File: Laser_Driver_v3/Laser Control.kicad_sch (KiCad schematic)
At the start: 10 parts, among them U2 AD5064BRUZ, U20 AD9833xRM, U35 AD9833xRM, U9 74AHCT125

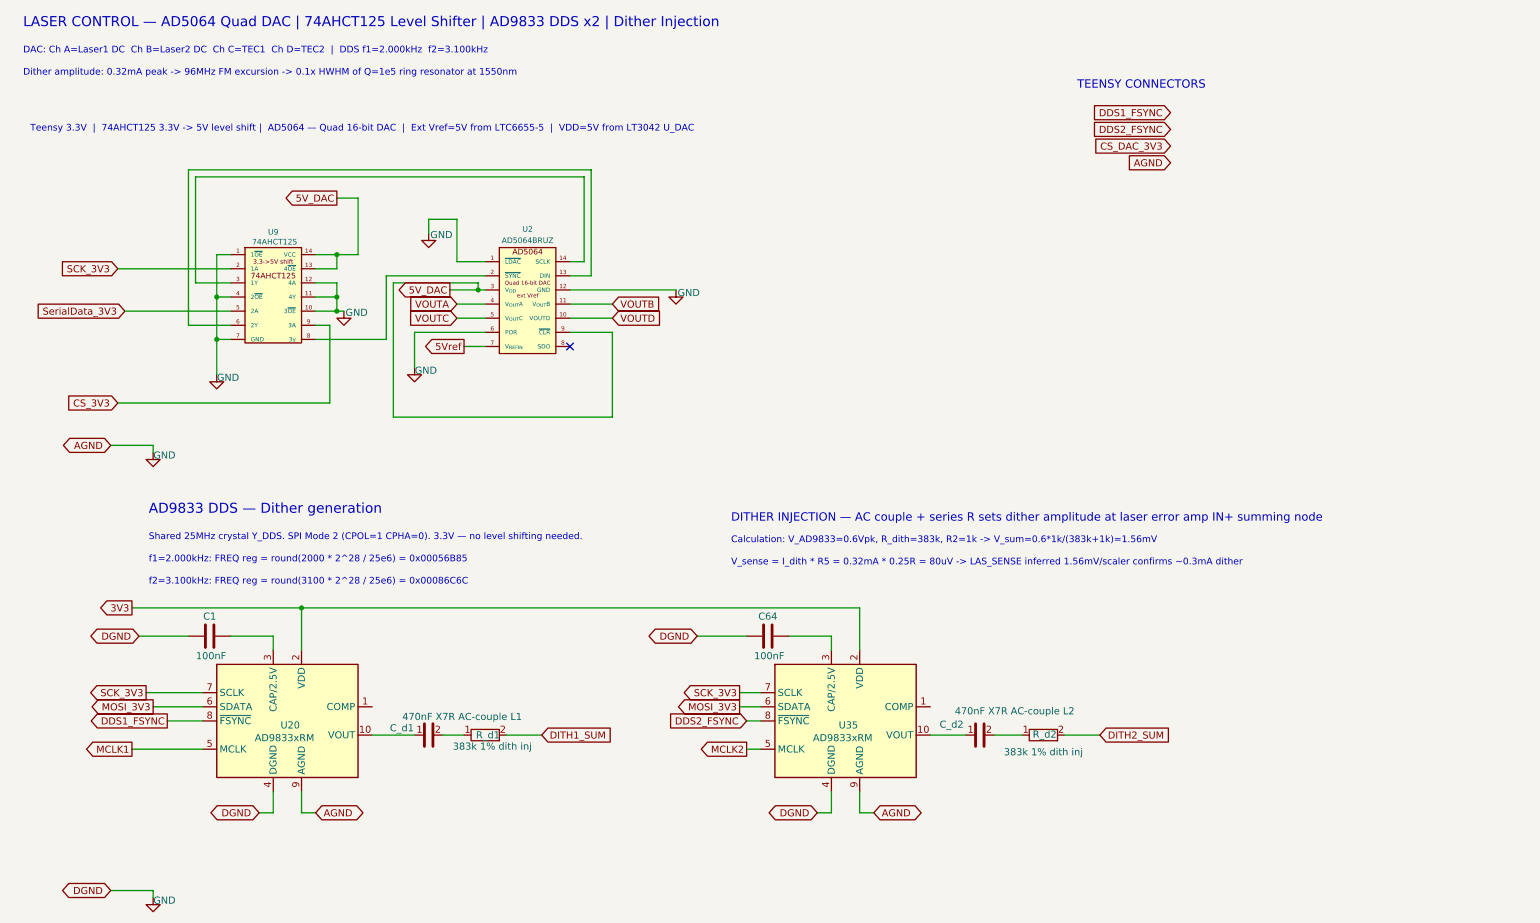
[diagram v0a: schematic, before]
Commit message: First full draft complete.  Added Teensy pinout sheet.
Used Copilot to generate firmware draft.  ** Still need to:  Recheck all specifications and pins, verify design with simulations, go through all footprints, create layout.
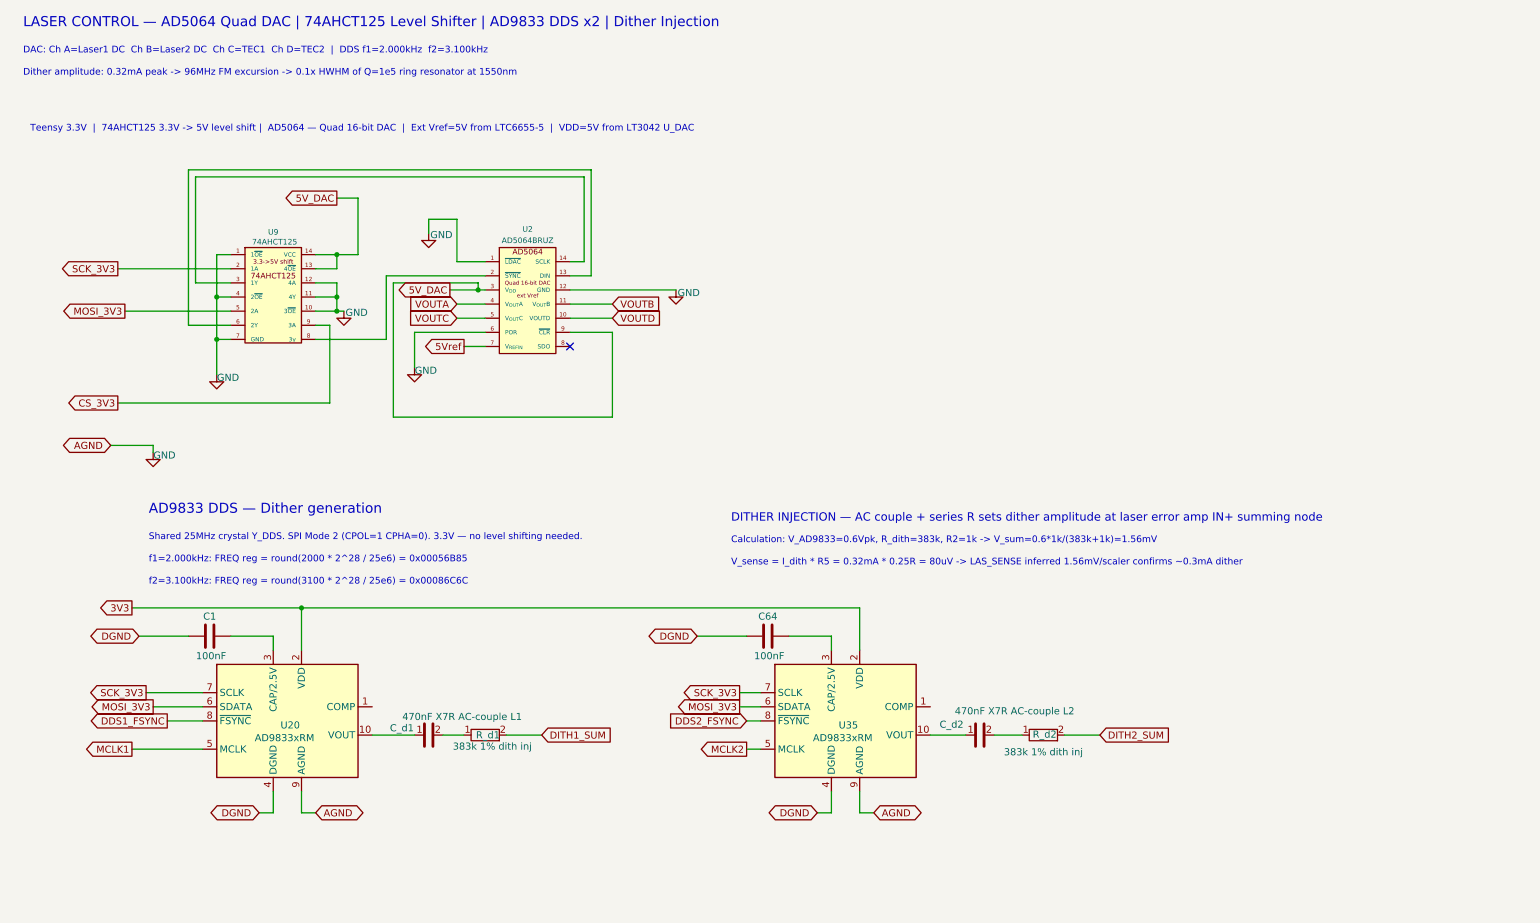
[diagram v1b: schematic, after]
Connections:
- net SerialData_3V3 is gone; now on net MOSI_3V3: U9.5 (2A)
- net GND: no longer C1.1, C64.1, U20.4 (DGND), U35.4 (DGND)
- new net DGND: C1.1, C64.1, U20.4 (DGND), U35.4 (DGND)
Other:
- note removed: "TEENSY CONNECTORS"
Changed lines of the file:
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@@
-		)
-	)
-	(text "TEENSY CONNECTORS"
-		(exclude_from_sim no)
-		(at 202.92 26.7 0)
-		(effects
-			(font
-				(size 1.5 1.5)
-			)
-			(justify left)
 		)
 	)
@@
 	(wire
 		(pts
-			(xy 29.21 171.45) (xy 36.83 171.45)
-		)
-		(stroke
-			(width 0)
-			(type default)
-		)
-	)
-	(wire
-		(pts
 			(xy 50.8 69.85) (xy 43.18 69.85)
 		)
@@
 	(wire
 		(pts
-			(xy 36.83 171.45) (xy 36.83 172.72)
-		)
-		(stroke
-			(width 0)
-			(type default)
-		)
-	)
-	(wire
-		(pts
 			(xy 142.24 135.89) (xy 146.05 135.89)
 		)
@@
 		)
 	)
-	(global_label "SerialData_3V3"
-		(shape input)
+	(global_label "MOSI_3V3"
+		(shape output)
 		(at 31.75 67.31 180)
 		(fields_autoplaced yes)
@@
 		)
 		(property "Intersheetrefs" "${INTERSHEET_REFS}"
-			(at 14.4926 67.31 0)
+			(at 19.6934 67.31 0)
 			(hide yes)
 			(show_name no)
@@
 		)
 	)
-	(global_label "DDS1_FSYNC"
-		(shape input)
-		(at 219.71 31.64 180)
-		(fields_autoplaced yes)
-		(effects
-			(font
-				(size 1.27 1.27)
-			)
-			(justify right)
-		)
-		(property "Intersheetrefs" "${INTERSHEET_REFS}"
-			(at 219.71 31.64 0)
-			(hide yes)
-			(show_name no)
-			(do_not_autoplace no)
-			(effects
-				(font
-					(size 1.27 1.27)
-				)
-				(justify right)
-			)
-		)
-	)
 	(global_label "5Vref"
 		(shape output)
@@
 	)
 	(global_label "CS_3V3"
-		(shape input)
+		(shape output)
 		(at 30.48 83.82 180)
 		(fields_autoplaced yes)
@@
 	)
 	(global_label "SCK_3V3"
-		(shape input)
+		(shape output)
 		(at 30.48 59.69 180)
 		(fields_autoplaced yes)
@@
 	(global_label "DDS2_FSYNC"
 		(shape input)
-		(at 219.71 34.64 180)
+		(at 143.51 140.97 180)
 		(fields_autoplaced yes)
 		(effects
@@
 		)
 		(property "Intersheetrefs" "${INTERSHEET_REFS}"
-			(at 219.71 34.64 0)
-			(hide yes)
-			(show_name no)
-			(do_not_autoplace no)
-			(effects
-				(font
-					(size 1.27 1.27)
-				)
-				(justify right)
-			)
-		)
-	)
-	(global_label "AGND"
-		(shape input)
-		(at 219.71 40.64 180)
-		(fields_autoplaced yes)
-		(effects
-			(font
-				(size 1.27 1.27)
-			)
-			(justify right)
-		)
-		(property "Intersheetrefs" "${INTERSHEET_REFS}"
-			(at 219.71 40.64 0)
-			(hide yes)
-			(show_name no)
-			(do_not_autoplace no)
-			(effects
-				(font
-					(size 1.27 1.27)
-				)
-				(justify right)
-			)
-		)
-	)
-	(global_label "DDS2_FSYNC"
-		(shape input)
-		(at 143.51 140.97 180)
-		(fields_autoplaced yes)
-		(effects
-			(font
-				(size 1.27 1.27)
-			)
-			(justify right)
-		)
-		(property "Intersheetrefs" "${INTERSHEET_REFS}"
 			(at 143.51 140.97 0)
-			(hide yes)
-			(show_name no)
-			(do_not_autoplace no)
-			(effects
-				(font
-					(size 1.27 1.27)
-				)
-				(justify right)
-			)
-		)
-	)
-	(global_label "DGND"
-		(shape bidirectional)
-		(at 29.21 171.45 180)
-		(fields_autoplaced yes)
-		(effects
-			(font
-				(size 1.27 1.27)
-			)
-			(justify right)
-		)
-		(property "Intersheetrefs" "${INTERSHEET_REFS}"
-			(at 19.973 171.45 0)
 			(hide yes)
 			(show_name no)
@@
 				)
 				(justify left)
-			)
-		)
-	)
-	(global_label "CS_DAC_3V3"
-		(shape input)
-		(at 219.71 37.64 180)
-		(fields_autoplaced yes)
-		(effects
-			(font
-				(size 1.27 1.27)
-			)
-			(justify right)
-		)
-		(property "Intersheetrefs" "${INTERSHEET_REFS}"
-			(at 219.71 37.64 0)
-			(hide yes)
-			(show_name no)
-			(do_not_autoplace no)
-			(effects
-				(font
-					(size 1.27 1.27)
-				)
-				(justify right)
 			)
 		)
@@
 					(unit 1)
 				)
-			)
-		)
-	)
-	(symbol
-		(lib_id "power:GND")
-		(at 36.83 172.72 0)
-		(unit 1)
-		(body_style 1)
-		(exclude_from_sim no)
-		(in_bom yes)
-		(on_board yes)
-		(in_pos_files yes)
-		(dnp no)
-		(property "Reference" "#PWR032"
-			(at 36.83 179.07 0)
-			(hide yes)
-			(show_name no)
-			(do_not_autoplace no)
-			(effects
-				(font
-					(size 1.27 1.27)
-				)
-			)
-		)
-		(property "Value" "GND"
-			(at 38.862 173.228 0)
-			(show_name no)
-			(do_not_autoplace no)
-			(effects
-				(font
-					(size 1.27 1.27)
-				)
-			)
-		)
-		(property "Footprint" ""
-			(at 36.83 172.72 0)
-			(hide yes)
-			(show_name no)
-			(do_not_autoplace no)
-			(effects
-				(font
-					(size 1.27 1.27)
-				)
-			)
-		)
-		(property "Datasheet" ""
-			(at 36.83 172.72 0)
-			(hide yes)
-			(show_name no)
-			(do_not_autoplace no)
-			(effects
-				(font
-					(size 1.27 1.27)
-				)
-			)
-		)
-		(property "Description" "Power symbol creates a global label with name \"GND\" , ground"
-			(at 36.83 172.72 0)
-			(hide yes)
-			(show_name no)
-			(do_not_autoplace no)
-			(effects
-				(font
-					(size 1.27 1.27)
-				)
-			)
-		)
-		(pin "1"
-		)
-		(instances
-			(project "laser_driver_v3"
-				(path "/b2c3d4e5-f6a7-8901-bcde-f12345678901/e4d7b089-62e9-414f-b4cc-abd1480c07cf"
-					(reference "#PWR032")
-					(unit 1)
-				)

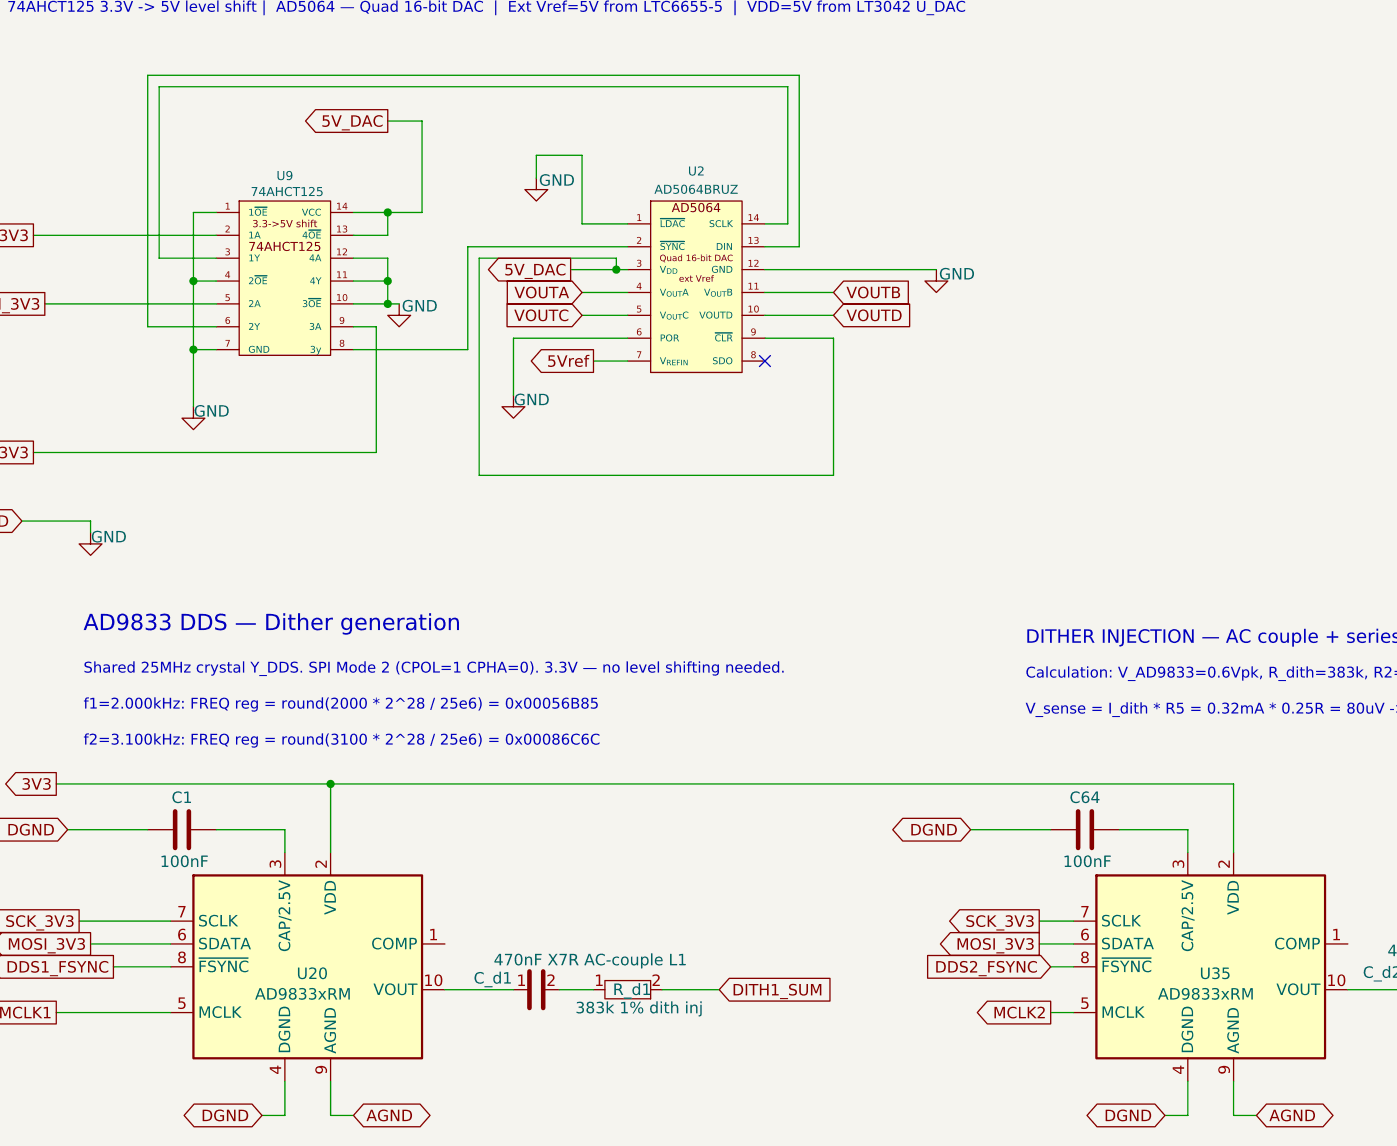
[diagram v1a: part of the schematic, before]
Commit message: Renumbered schematics, corrections, power verified
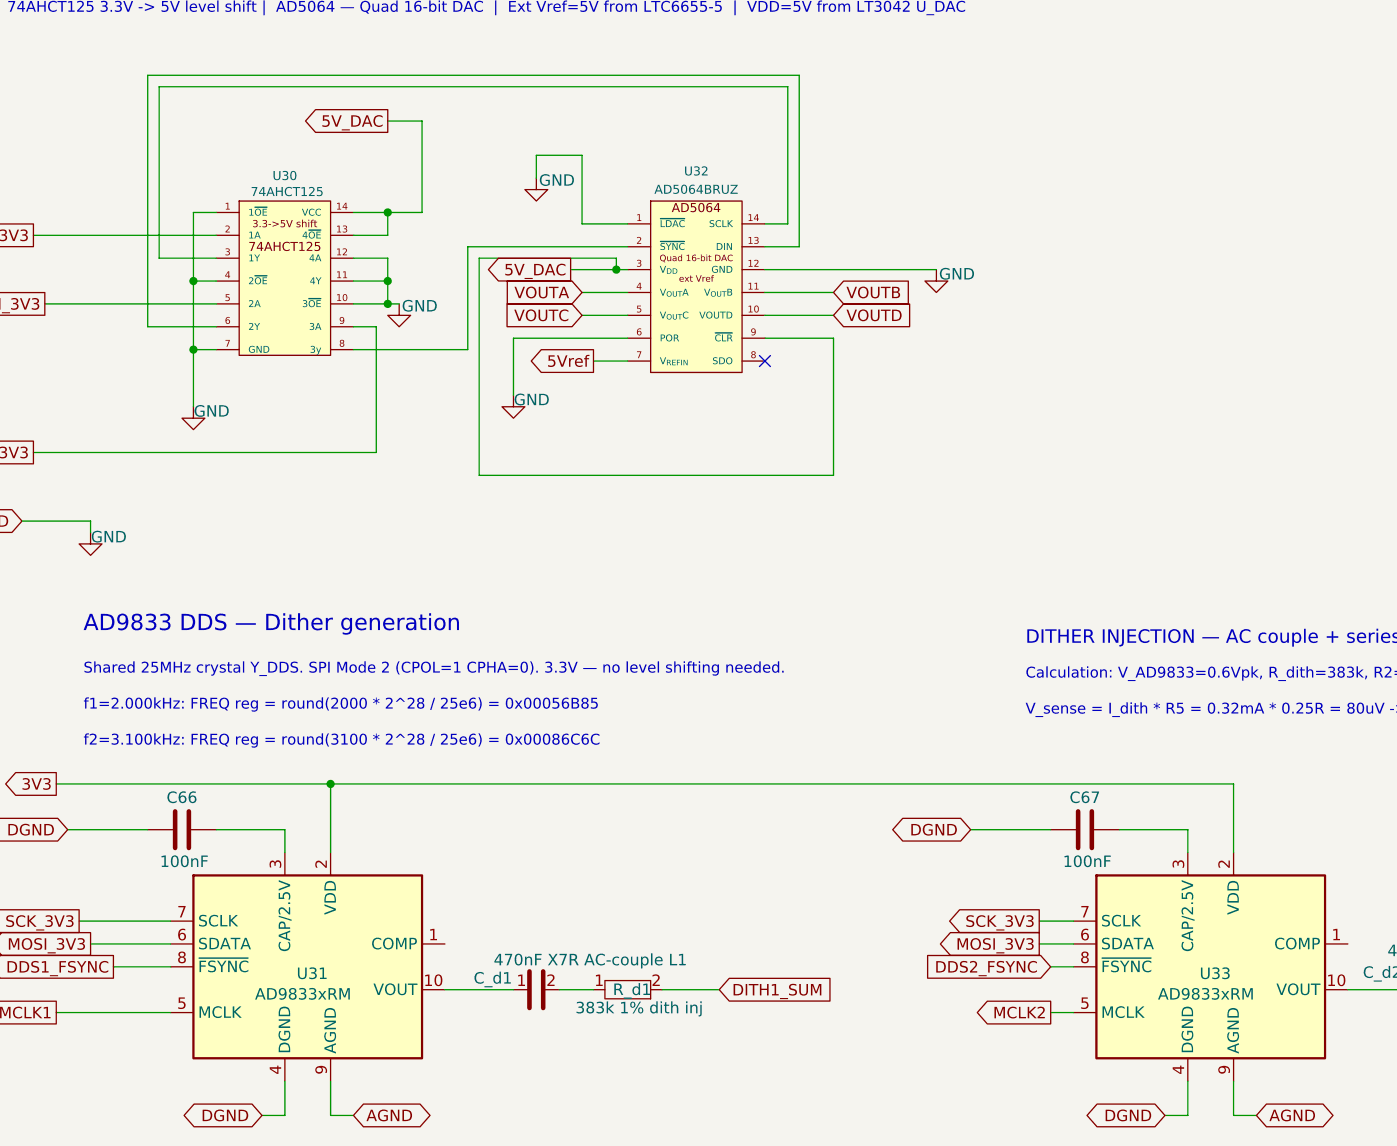
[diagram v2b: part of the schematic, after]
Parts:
- renumbered C1 to C66, C64 to C67, U9 to U30, U20 to U31, U2 to U32, U35 to U33
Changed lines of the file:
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@@
 		(in_pos_files yes)
 		(dnp no)
-		(property "Reference" "#PWR025"
+		(property "Reference" "#PWR027"
 			(at 48.26 85.09 0)
 			(hide yes)
@@
 			(project "laser_driver_v3"
 				(path "/b2c3d4e5-f6a7-8901-bcde-f12345678901/e4d7b089-62e9-414f-b4cc-abd1480c07cf"
-					(reference "#PWR025")
+					(reference "#PWR027")
 					(unit 1)
 				)
@@
 		(in_pos_files yes)
 		(dnp no)
-		(property "Reference" "#PWR024"
+		(property "Reference" "#PWR026"
 			(at 36.83 99.06 0)
 			(hide yes)
@@
 			(project "laser_driver_v3"
 				(path "/b2c3d4e5-f6a7-8901-bcde-f12345678901/e4d7b089-62e9-414f-b4cc-abd1480c07cf"
-					(reference "#PWR024")
+					(reference "#PWR026")
 					(unit 1)
 				)
@@
 		(in_pos_files yes)
 		(dnp no)
-		(property "Reference" "#PWR033"
+		(property "Reference" "#PWR029"
 			(at 83.82 83.82 0)
 			(hide yes)
@@
 			(project "laser_driver_v3"
 				(path "/b2c3d4e5-f6a7-8901-bcde-f12345678901/e4d7b089-62e9-414f-b4cc-abd1480c07cf"
-					(reference "#PWR033")
+					(reference "#PWR029")
 					(unit 1)
 				)
@@
 		(in_pos_files yes)
 		(dnp no)
-		(property "Reference" "U20"
+		(property "Reference" "U31"
 			(at 61.468 141.732 0)
 			(show_name no)
@@
 			(project "laser_driver_v3"
 				(path "/b2c3d4e5-f6a7-8901-bcde-f12345678901/e4d7b089-62e9-414f-b4cc-abd1480c07cf"
-					(reference "U20")
+					(reference "U31")
 					(unit 1)
 				)
@@
 		(in_pos_files yes)
 		(dnp no)
-		(property "Reference" "#PWR023"
+		(property "Reference" "#PWR031"
 			(at 130.81 69.85 0)
 			(hide yes)
@@
 			(project "laser_driver_v3"
 				(path "/b2c3d4e5-f6a7-8901-bcde-f12345678901/e4d7b089-62e9-414f-b4cc-abd1480c07cf"
-					(reference "#PWR023")
+					(reference "#PWR031")
 					(unit 1)
 				)
@@
 		(in_pos_files yes)
 		(dnp no)
-		(property "Reference" "U2"
+		(property "Reference" "U32"
 			(at 104.14 52.578 0)
 			(show_name no)
@@
 			(project "laser_driver_v3"
 				(path "/b2c3d4e5-f6a7-8901-bcde-f12345678901/e4d7b089-62e9-414f-b4cc-abd1480c07cf"
-					(reference "U2")
+					(reference "U32")
 					(unit 1)
 				)
@@
 		(in_pos_files yes)
 		(dnp no)
-		(property "Reference" "#PWR022"
+		(property "Reference" "#PWR028"
 			(at 71.12 73.66 0)
 			(hide yes)
@@
 			(project "laser_driver_v3"
 				(path "/b2c3d4e5-f6a7-8901-bcde-f12345678901/e4d7b089-62e9-414f-b4cc-abd1480c07cf"
-					(reference "#PWR022")
+					(reference "#PWR028")
 					(unit 1)
 				)
@@
 		(in_pos_files yes)
 		(dnp no)
-		(property "Reference" "C64"
+		(property "Reference" "C67"
 			(at 147.32 122.174 90)
 			(show_name no)
@@
 			(project "laser_driver_v3"
 				(path "/b2c3d4e5-f6a7-8901-bcde-f12345678901/e4d7b089-62e9-414f-b4cc-abd1480c07cf"
-					(reference "C64")
+					(reference "C67")
 					(unit 1)
 				)
@@
 		(in_pos_files yes)
 		(dnp no)
-		(property "Reference" "U9"
+		(property "Reference" "U30"
 			(at 58.42 53.086 0)
 			(show_name no)
@@
 			(project "laser_driver_v3"
 				(path "/b2c3d4e5-f6a7-8901-bcde-f12345678901/e4d7b089-62e9-414f-b4cc-abd1480c07cf"
-					(reference "U9")
+					(reference "U30")
 					(unit 1)
 				)
@@
 		(in_pos_files yes)
 		(dnp no)
-		(property "Reference" "C1"
+		(property "Reference" "C66"
 			(at 46.99 122.174 90)
 			(show_name no)
@@
 			(project "laser_driver_v3"
 				(path "/b2c3d4e5-f6a7-8901-bcde-f12345678901/e4d7b089-62e9-414f-b4cc-abd1480c07cf"
-					(reference "C1")
+					(reference "C66")
 					(unit 1)
 				)
@@
 		(in_pos_files yes)
 		(dnp no)
-		(property "Reference" "U35"
+		(property "Reference" "U33"
 			(at 161.798 141.732 0)
 			(show_name no)
@@
 			(project "laser_driver_v3"
 				(path "/b2c3d4e5-f6a7-8901-bcde-f12345678901/e4d7b089-62e9-414f-b4cc-abd1480c07cf"
-					(reference "U35")
+					(reference "U33")
 					(unit 1)
 				)
@@
 		(in_pos_files yes)
 		(dnp no)
-		(property "Reference" "#PWR02"
+		(property "Reference" "#PWR030"
 			(at 86.36 59.69 0)
 			(hide yes)
@@
 			(project "laser_driver_v3"
 				(path "/b2c3d4e5-f6a7-8901-bcde-f12345678901/e4d7b089-62e9-414f-b4cc-abd1480c07cf"
-					(reference "#PWR02")
-					(unit 1)
-				)
+					(reference "#PWR030")
+					(unit 1)
+				)
